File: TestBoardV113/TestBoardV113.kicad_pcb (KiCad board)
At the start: 2 copper layers, 81.1 x 79.4 mm, 76 parts, among them J1 Conn_01x02_Socket, J10 Conn_01x02_Pin, J11 Conn_01x02_Pin, J12 Conn_02x03_Odd_Even, J13 Conn_01x01_Pin, J14 Conn_01x28_Socket, J15 Conn_01x01_Pin, J16 Conn_01x01_Pin, J17 Conn_01x02_Pin, J18 Conn_01x02_Socket, J19 Conn_01x28_Socket, J2 Conn_02x06_Odd_Even, J20 Conn_01x01_Pin, J21 Conn_01x02_Pin, J22 Conn_02x03_Odd_Even, J23 Conn_01x02_Pin, J24 Conn_01x02_Socket, J3 Conn_01x02_Pin, J4 Conn_01x02_Pin, J5 Conn_01x02_Pin, J6 Conn_01x02_Pin, J7 Conn_01x02_Pin, J8 Conn_01x02_Pin, J9 Conn_01x02_Pin, SW1 SW_DIP_x04, U3 NCP705MTADJTCG, U4 TAR5SxxU_SOT353F, U5 TXB0104PW, U6 TXB0104PW

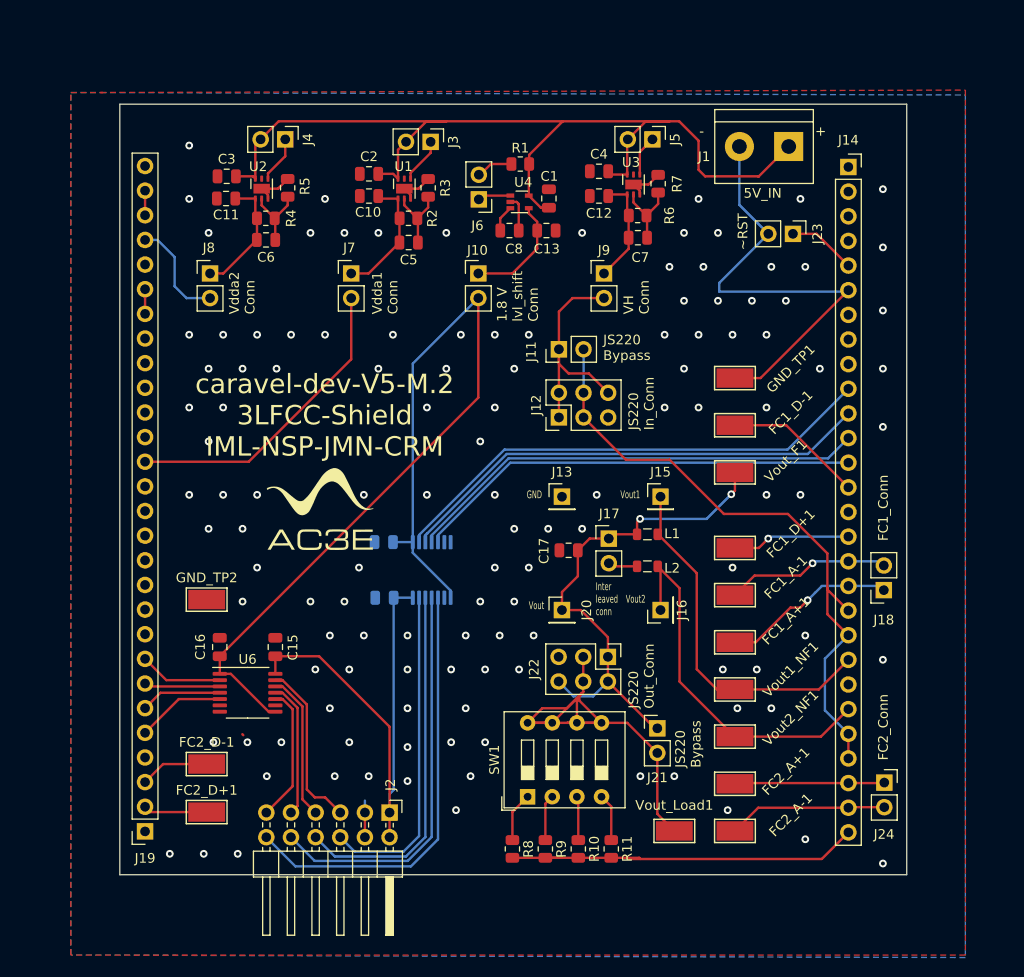
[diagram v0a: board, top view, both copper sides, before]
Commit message: Added features
Added Joulescope port for efficiency measurement with and without level shifters
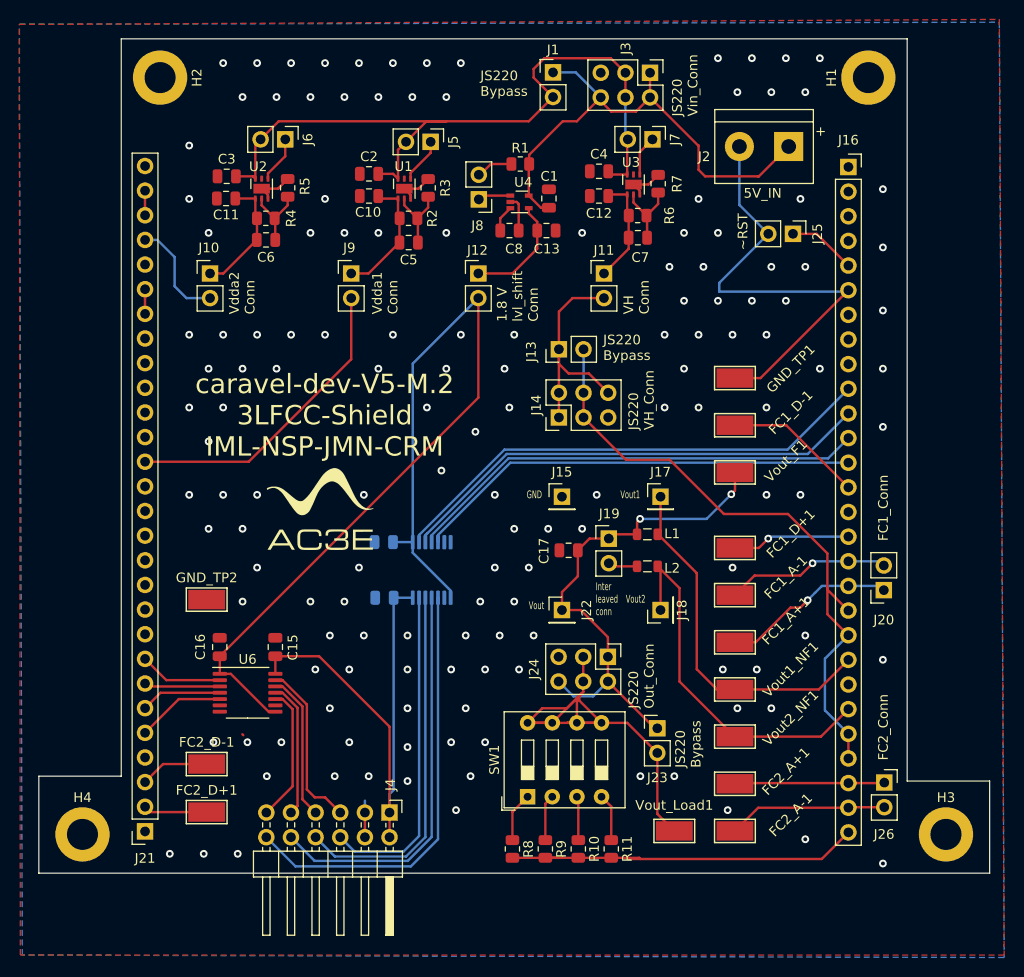
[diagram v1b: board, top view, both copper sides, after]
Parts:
- added H1: MountingHole_Pad, MountingHole:MountingHole_3.2mm_M3_DIN965_Pad, F.Cu at (180.5, 48.5)
- added H2: MountingHole_Pad, MountingHole:MountingHole_3.2mm_M3_DIN965_Pad, F.Cu at (107.5, 48.5)
- added H3: MountingHole_Pad, MountingHole:MountingHole_3.2mm_M3_DIN965_Pad, F.Cu at (188.5, 126.5)
- added H4: MountingHole_Pad, MountingHole:MountingHole_3.2mm_M3_DIN965_Pad, F.Cu at (99.5, 126.5)
- added J1: Conn_01x02_Pin, Connector_PinHeader_2.54mm:PinHeader_1x02_P2.54mm_Vertical, F.Cu at (148.0, 48.0)
- added J3: Conn_02x03_Odd_Even, Connector_PinHeader_2.54mm:PinHeader_2x03_P2.54mm_Vertical, F.Cu at (158.0, 48.0)
- renumbered J8 to J10, J9 to J11, J10 to J12, J11 to J13, J12 to J14, J13 to J15, J14 to J16, J15 to J17, J16 to J18, J17 to J19, J1 to J2, J18 to J20, J19 to J21, J20 to J22, J21 to J23, J22 to J24, J23 to J25, J24 to J26, J2 to J4, J3 to J5, J4 to J6, J5 to J7, J6 to J8, J7 to J9
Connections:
- C2 pad 1: VCC -> VH/VDDA1-2_Power
- C3 pad 1: VCC -> VH/VDDA1-2_Power
- C4 pad 1: VCC -> VH/VDDA1-2_Power
- J5 pad 2: VCC -> VH/VDDA1-2_Power
- J6 pad 2: VCC -> VH/VDDA1-2_Power
- J7 pad 2: VCC -> VH/VDDA1-2_Power
- U1 pad 6: VCC -> VH/VDDA1-2_Power
- U2 pad 6: VCC -> VH/VDDA1-2_Power
- U3 pad 6: VCC -> VH/VDDA1-2_Power
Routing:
- net VH/VDDA1-2_Power: track 0.00 -> 77.7 mm
- net VCC: track 101.0 -> 52.2 mm
- net GND: vias 122 -> 143
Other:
- board size 81.1 x 79.4 mm -> 98 x 86 mm
- board text added: "JS220 VH_Conn"
- board text added: "JS220 Vin_Conn"
- board text removed: "-"
- board text removed: "JS220 In_Conn"
